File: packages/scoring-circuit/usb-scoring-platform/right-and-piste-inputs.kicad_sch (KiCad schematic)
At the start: 20 parts, among them J4 RIGHT WEAPON A B C, J5 PISTE - NOT protective earth, U9 SN74LVC125APWR

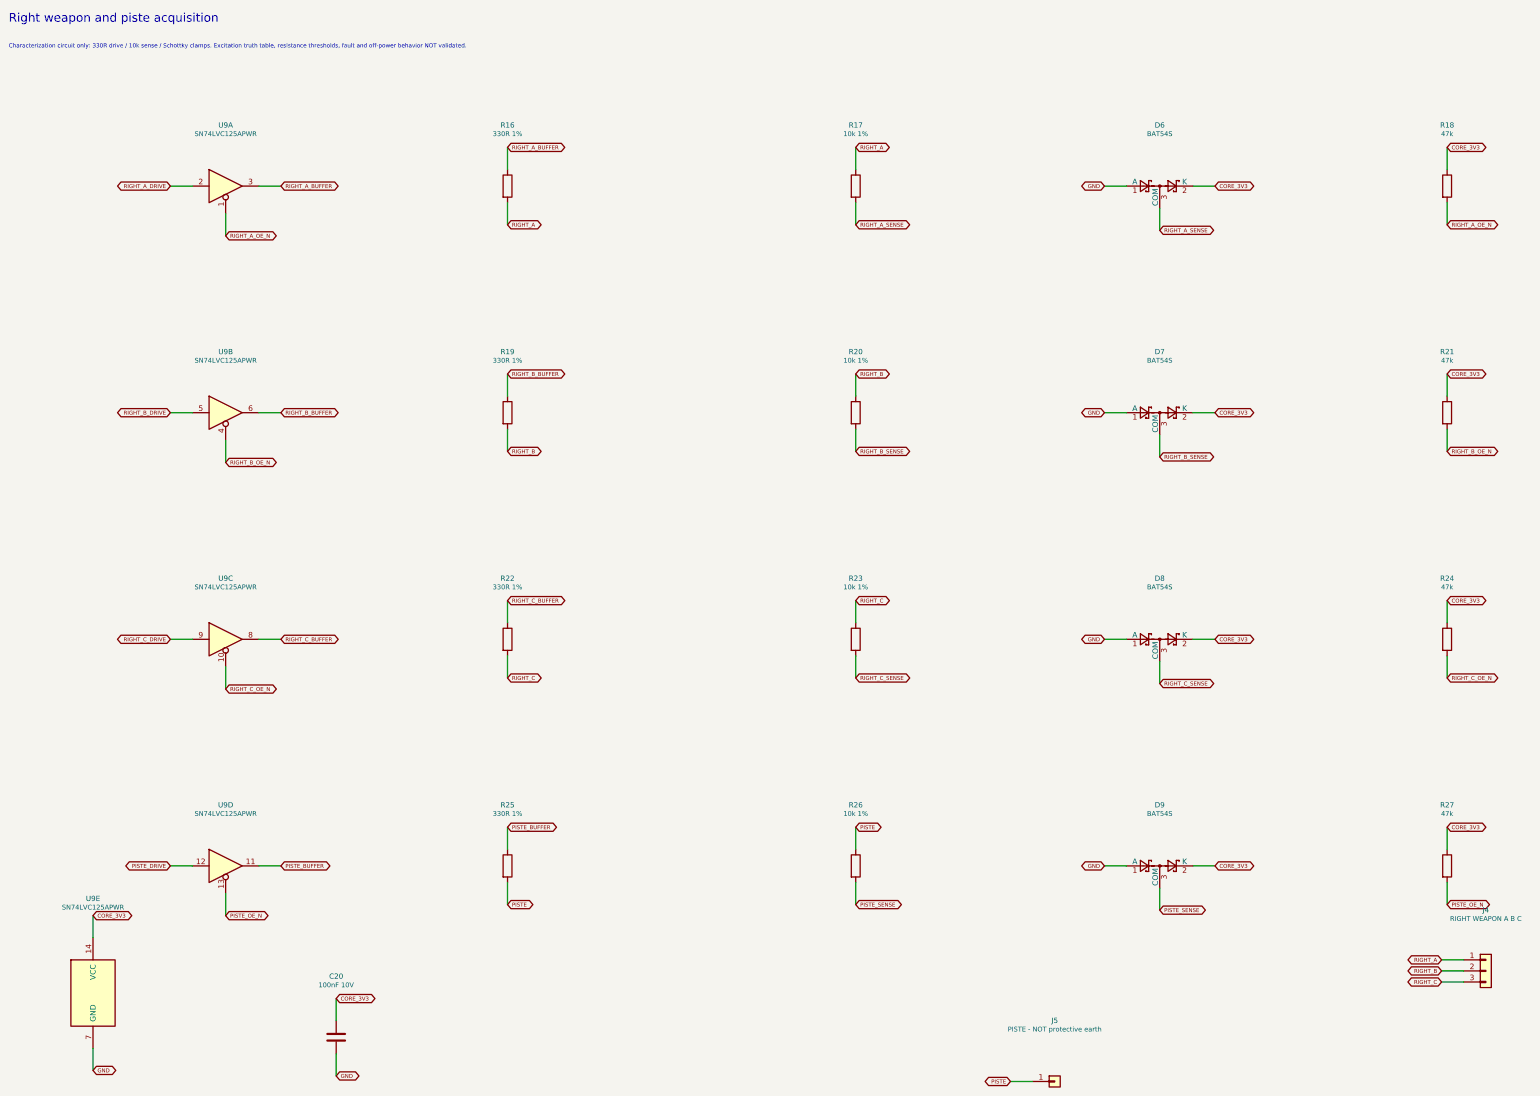
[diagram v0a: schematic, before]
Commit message: fix(scoring-circuit): strengthen STM32 sensing bias and model continuity
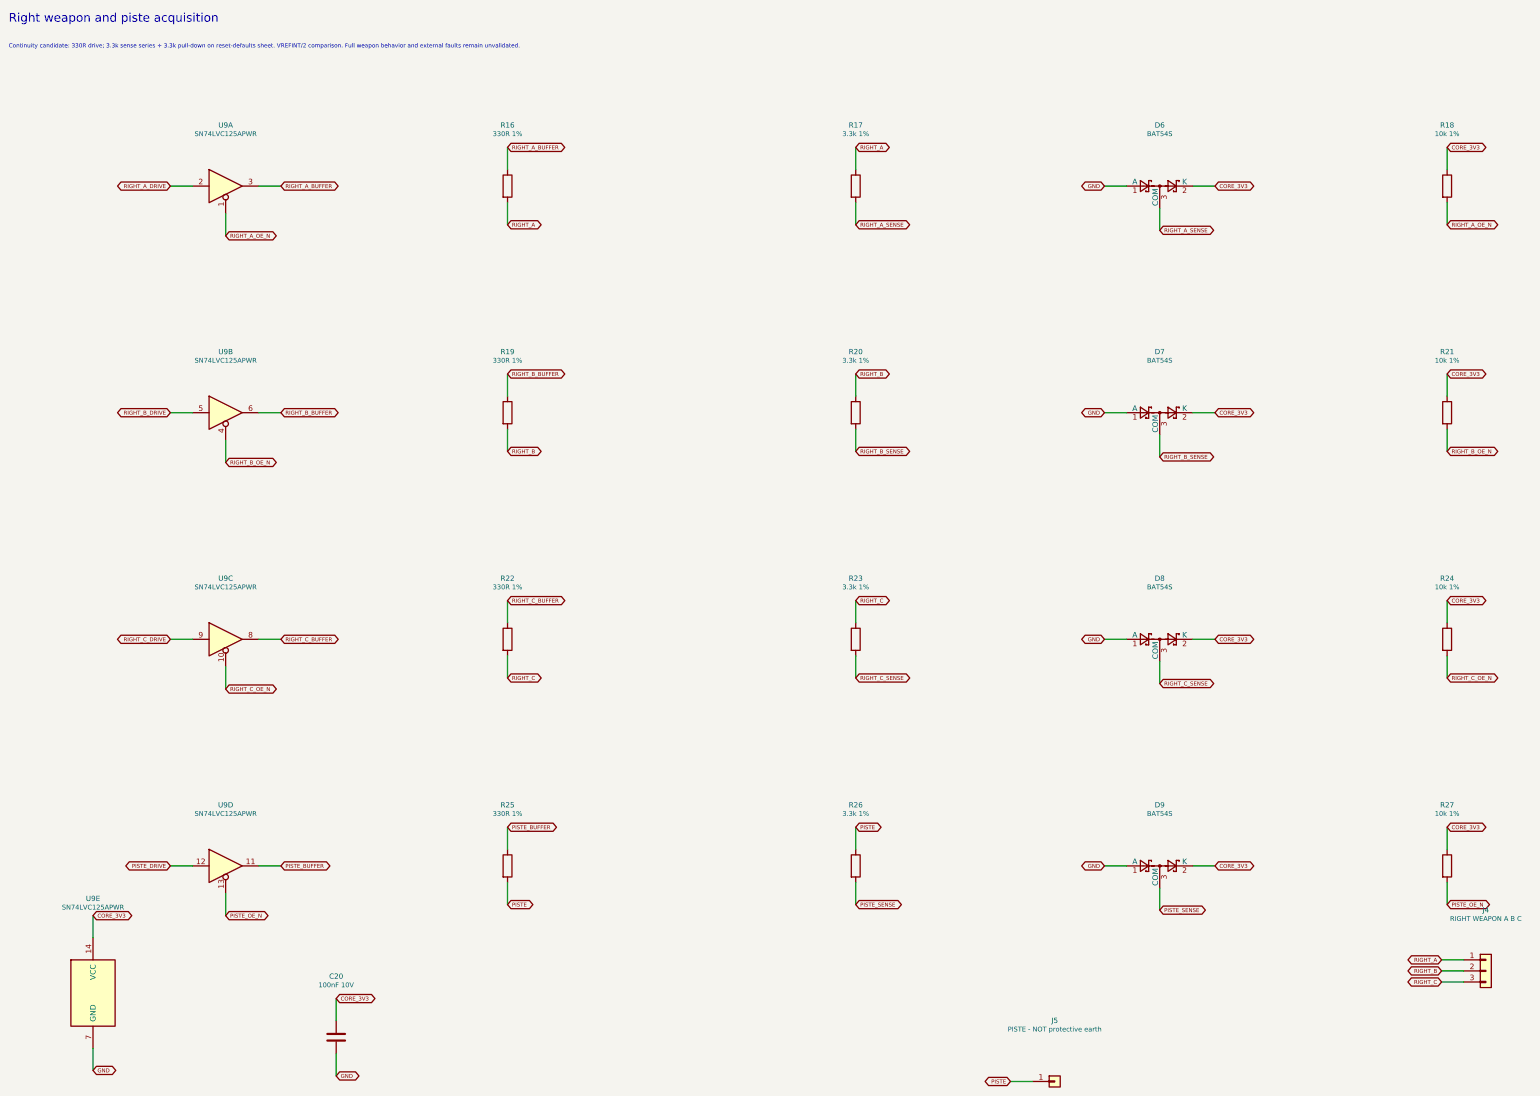
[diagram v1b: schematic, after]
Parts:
- R17, R20, R23, R26: value 10k 1% -> 3.3k 1%
- R18, R21, R24, R27: value 47k -> 10k 1%
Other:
- note added: "Continuity candidate: 330R drive; 3.3k sense series + 3.3k pull-down on reset-defaults sheet. VREFINT/2 comparison. Full weapon behavior and external faults remain unvalidated."
- note removed: "Characterization circuit only: 330R drive / 10k sense / Schottky clamps. Excitation truth table, resistance thresholds, fault and off-power behavior NOT validated."

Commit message: fix(scoring-circuit): improve excitation margin and power-off behavior
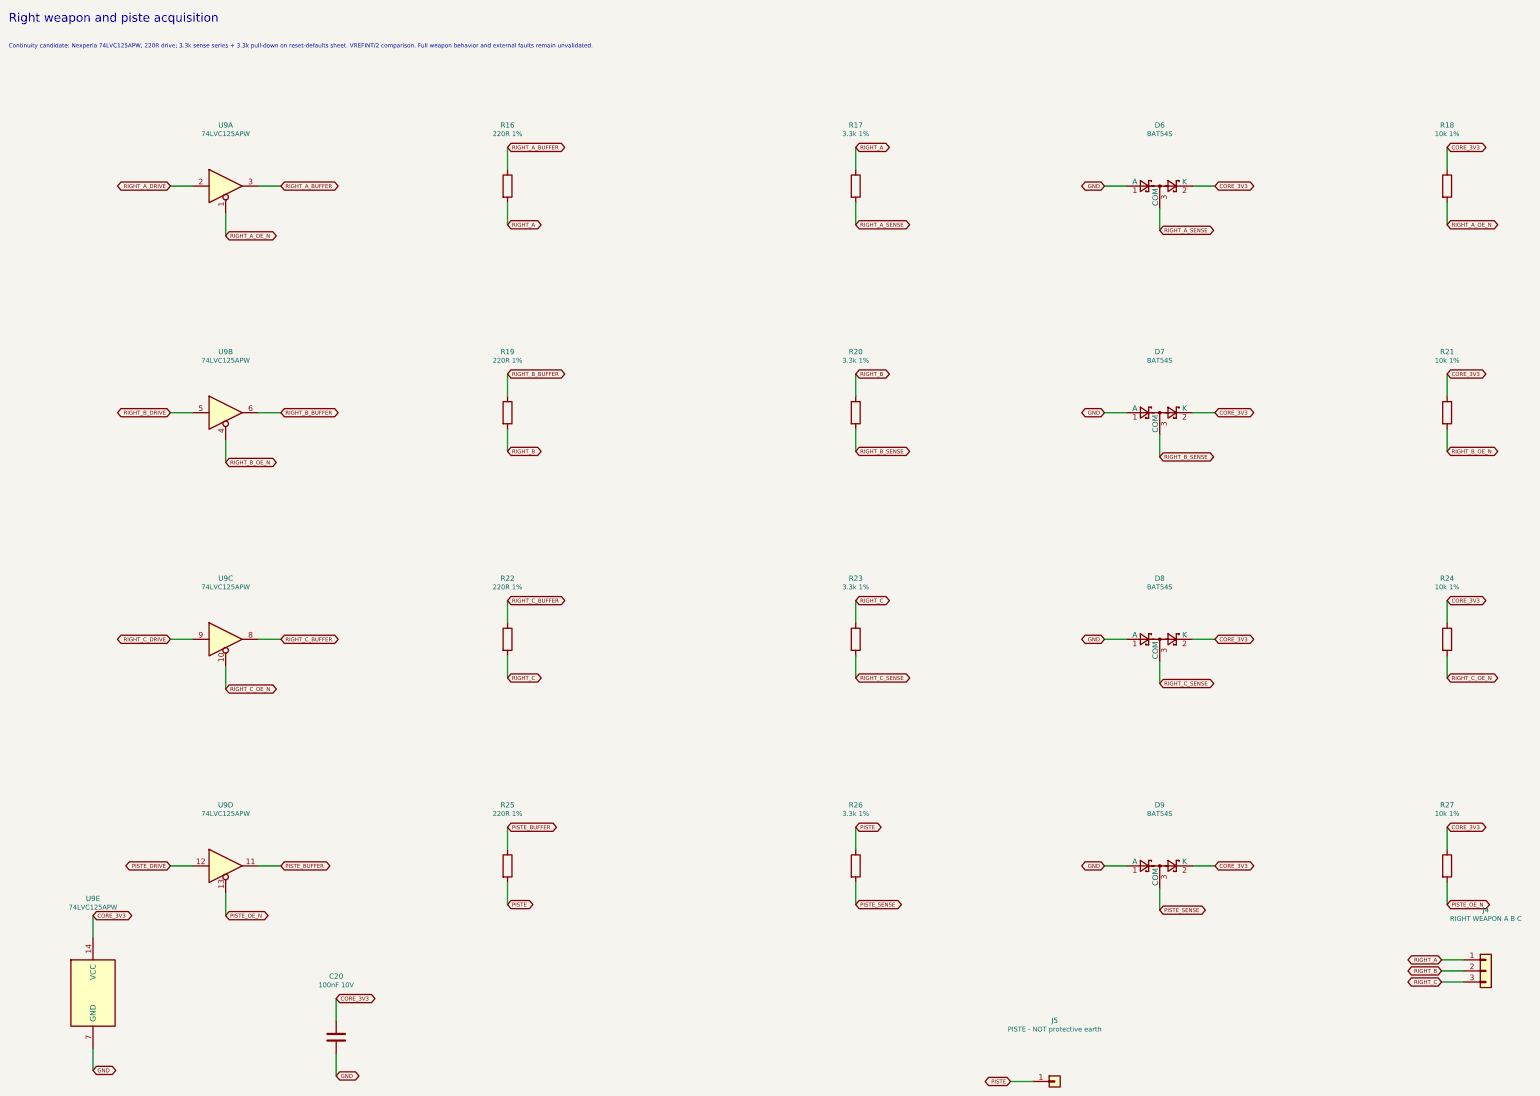
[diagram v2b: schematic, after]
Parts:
- R16, R19, R22, R25: value 330R 1% -> 220R 1%
- U9: value SN74LVC125APWR -> 74LVC125APW; Manufacturer (none) -> Nexperia
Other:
- note added: "Continuity candidate: Nexperia 74LVC125APW, 220R drive; 3.3k sense series + 3.3k pull-down on reset-defaults sheet. VREFINT/2 comparison. Full weapon behavior and external faults remain unvalidated."
- note removed: "Continuity candidate: 330R drive; 3.3k sense series + 3.3k pull-down on reset-defaults sheet. VREFINT/2 comparison. Full weapon behavior and external faults remain unvalidated."

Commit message: feat(scoring-circuit): select exact prototype resistor parts
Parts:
- R16, R19, R22, R25: MPN (none) -> ERJPA3F2200V; Manufacturer (none) -> Panasonic
- R17, R20, R23, R26: MPN (none) -> RC0603FR-073K3L; Manufacturer (none) -> YAGEO
- R18, R21, R24, R27: MPN (none) -> RC0603FR-0710KL; Manufacturer (none) -> YAGEO

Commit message: feat(scoring-circuit): select bypass and timing capacitors
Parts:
- C20: MPN (none) -> C1608X7R1H104K080AA; Manufacturer (none) -> TDK

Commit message: feat(scoring-circuit): bind diode selections and review polarity
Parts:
- D6, D7, D8, D9: MPN (none) -> BAT54S,215; Manufacturer (none) -> Nexperia

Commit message: fix(scoring-circuit): select service headers and correct drill sizes
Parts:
- J4: footprint Connector_PinHeader_2.54mm:PinHeader_1x03_P2.54mm_Vertical -> ScoringPlatform:Samtec_HTSW-103-07-L-S; MPN (none) -> HTSW-103-07-L-S; Manufacturer (none) -> Samtec
- J5: footprint Connector_PinHeader_2.54mm:PinHeader_1x01_P2.54mm_Vertical -> ScoringPlatform:Samtec_HTSW-101-07-L-S; MPN (none) -> HTSW-101-07-L-S; Manufacturer (none) -> Samtec

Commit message: chore(scoring-circuit): complete assembly BOM ordering fields
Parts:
- U9: MPN (none) -> 74LVC125APW

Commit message: fix(scoring-circuit): specify orderable sensing buffers
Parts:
- U9: MPN 74LVC125APW -> 74LVC125APW,118
